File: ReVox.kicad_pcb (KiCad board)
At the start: 2 copper layers, 60.8 x 86.2 mm, 42 parts, among them CN1 EXPANSION_PORT, CN2 RAW_OUT, CN3 AMP_OUT, CN4 CN_RAW_DAC, U1 GAL20V8, U2 74LS273, U3 TLC272

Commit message: RV1 -> 500k
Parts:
- RV1: value 470k -> 500k

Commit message: C8 -> 1uF
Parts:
- C8: value 10u -> 1u

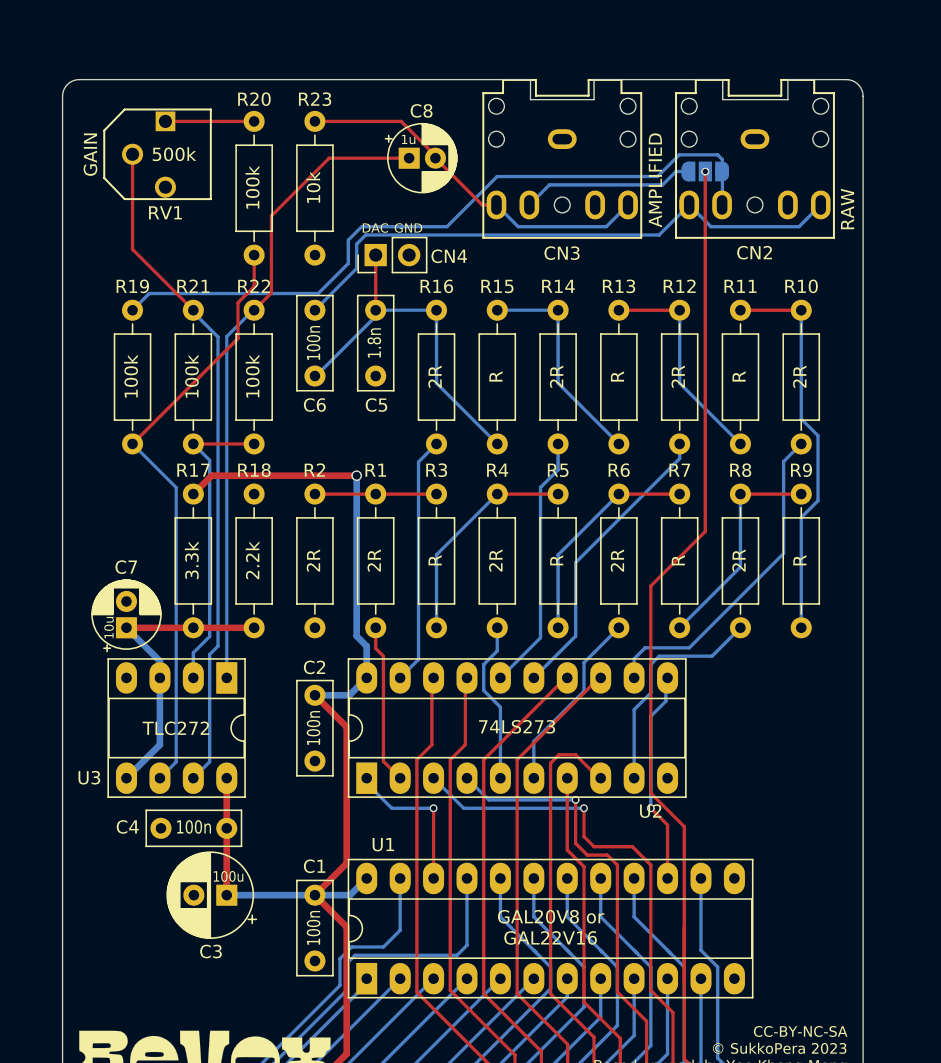
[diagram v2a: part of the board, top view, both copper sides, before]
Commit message: Remove amplified output jack This makes the opamp oscillate and is totally unnecessary
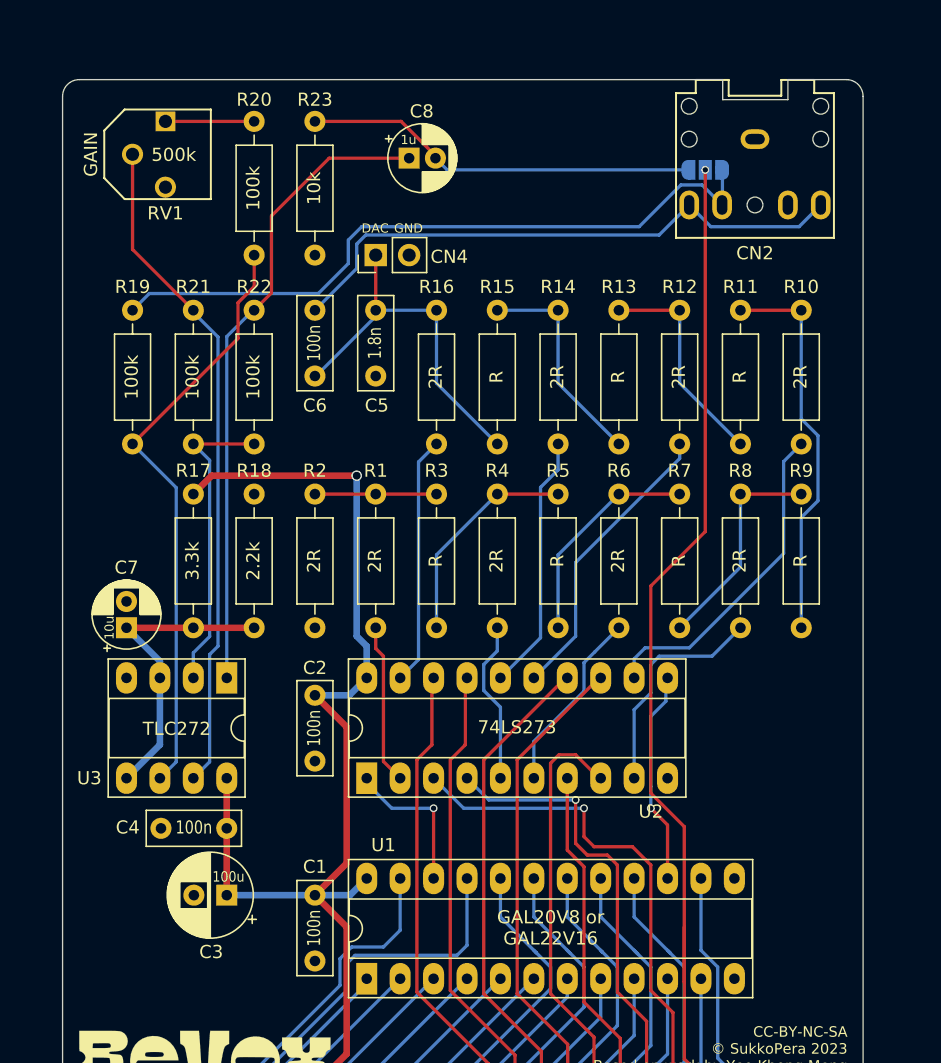
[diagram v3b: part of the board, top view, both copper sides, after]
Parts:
- removed CN3: AMP_OUT, ReVox:AudioJack_SJ1-3525N
- moved JP1 0.13 mm to (170.6, 68.7)
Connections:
- JP1 pad 1: Net-(CN3-PadTN) -> /amplified_audio
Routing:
- net Net-(CN3-PadTN): track 13.1 -> 0.00 mm
- net /amplified_audio: track 27.9 -> 30.1 mm
- net /amplifier_in: track 54.4 -> 53.0 mm
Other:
- outline, holes or cut-outs redrawn
- board text removed: "AMPLIFIED"

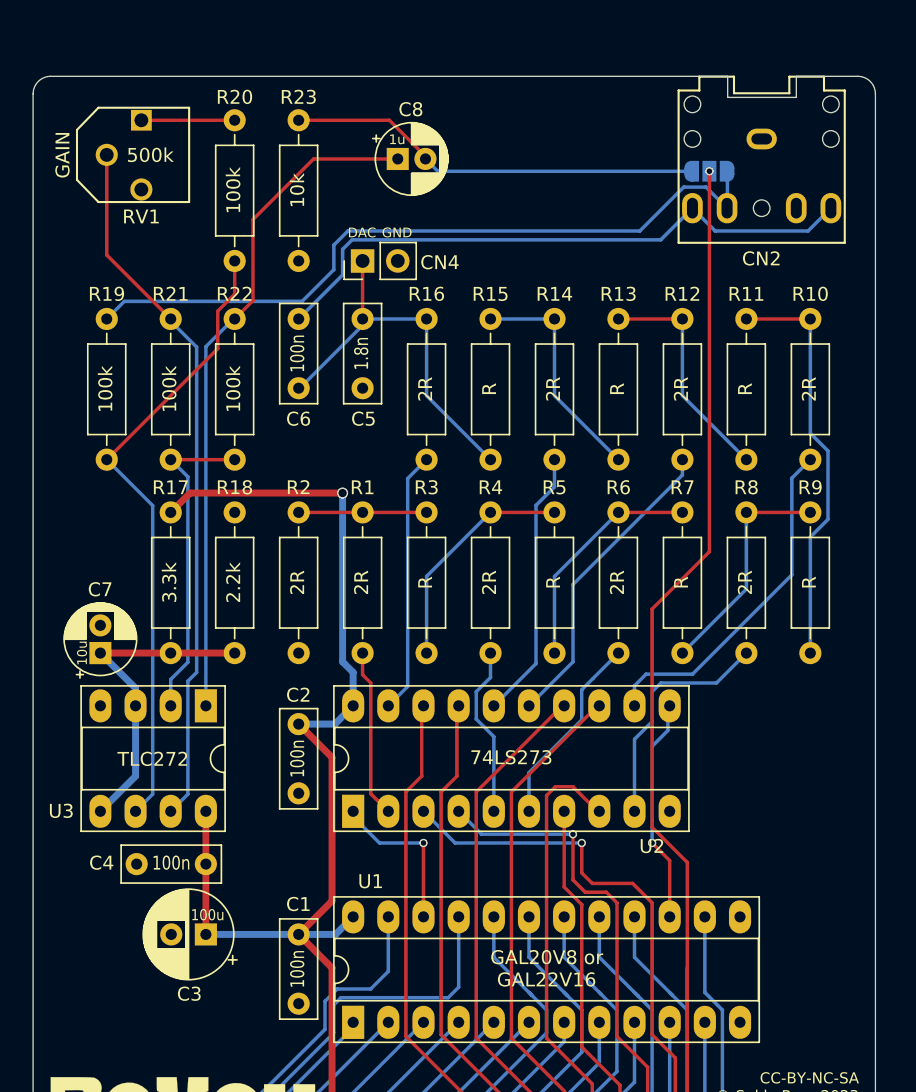
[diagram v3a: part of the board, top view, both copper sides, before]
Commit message: Some rerouting
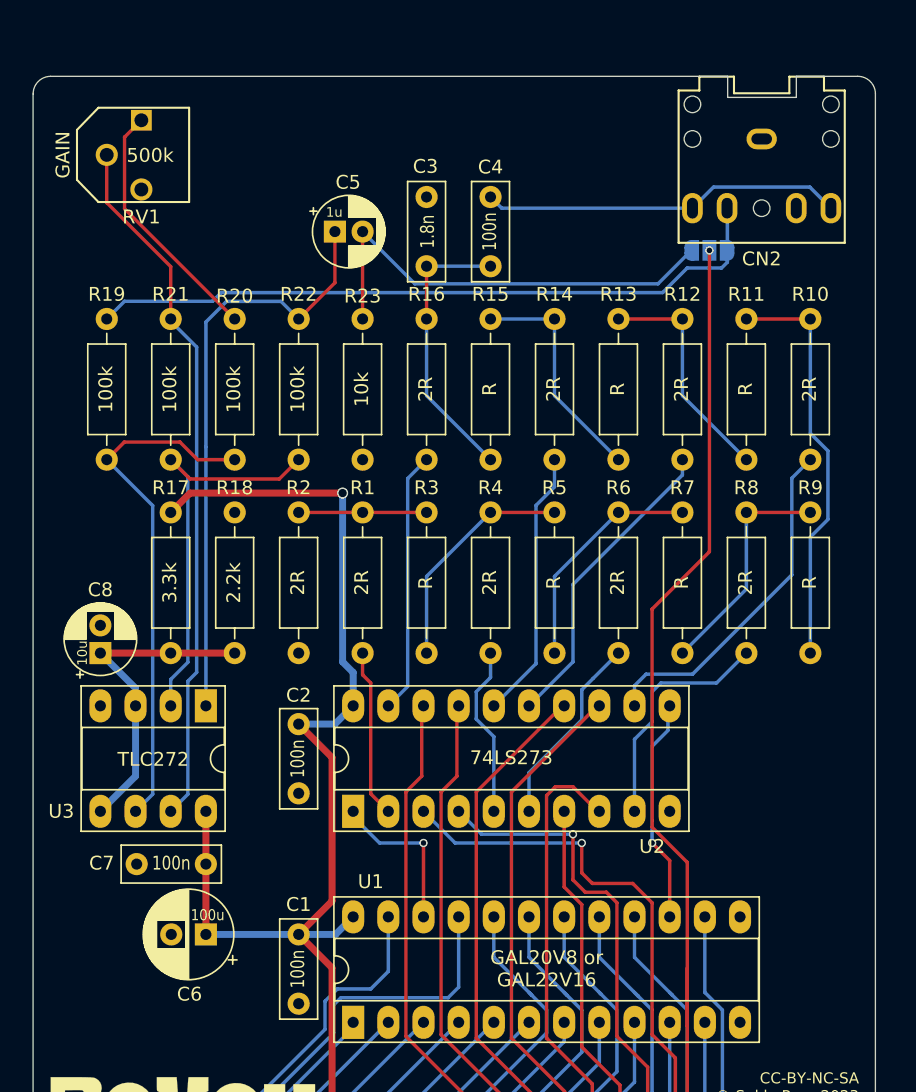
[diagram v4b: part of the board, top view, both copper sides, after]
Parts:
- removed CN4: CN_RAW_DAC, Connector_PinHeader_2.54mm:PinHeader_1x02_P2.54mm_Vertical
- moved C4 16.4 mm to (154.8, 70.6)
- moved R23 15.1 mm to (145.6, 79.4)
- moved C3 14.6 mm to (150.2, 70.6), turned to 270 degrees
- moved R20 14.4 mm to (136.4, 79.4)
- moved C5 6.94 mm to (143.6, 73.1)
- moved JP1 5.72 mm to (170.6, 74.4)
- moved R22 4.62 mm to (141.0, 79.4)
- renumbered C5 to C3, C6 to C4, C8 to C5, C3 to C6, C4 to C7, C7 to C8
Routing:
- net /analog_audio: track 44.2 -> 26.2 mm
- net Net-(R20-Pad1): track 6.74 -> 18.2 mm
- net Net-(R19-Pad1): track 45.5 -> 37.6 mm
- net Net-(C3-Pad2): track 27.8 -> 20.5 mm
- net Net-(R21-Pad2): track 23.4 -> 29.2 mm
- net /ext_audio: track 83.6 -> 77.9 mm
- net Net-(C5-Pad1): track 48.3 -> 43.0 mm
- net /amplified_audio: track 30.1 -> 32.6 mm
- net /amplifier_in: track 53.0 -> 50.4 mm
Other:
- board text removed: "DAC"
- board text removed: "GND"

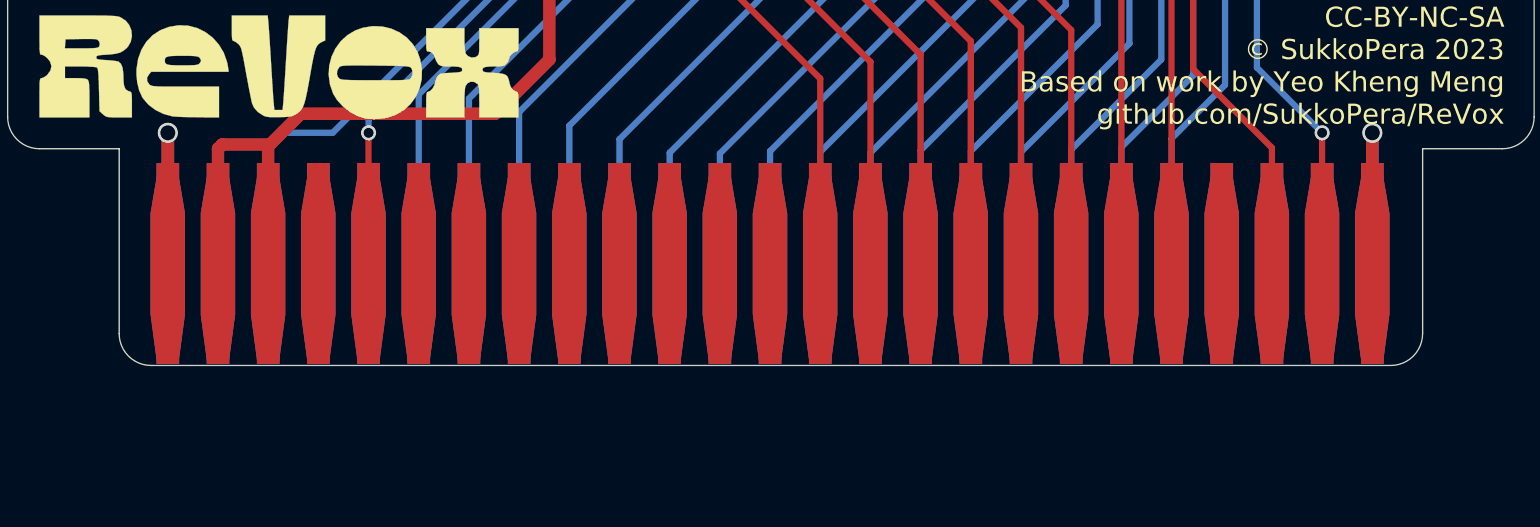
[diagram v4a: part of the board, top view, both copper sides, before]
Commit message: Update edge connector
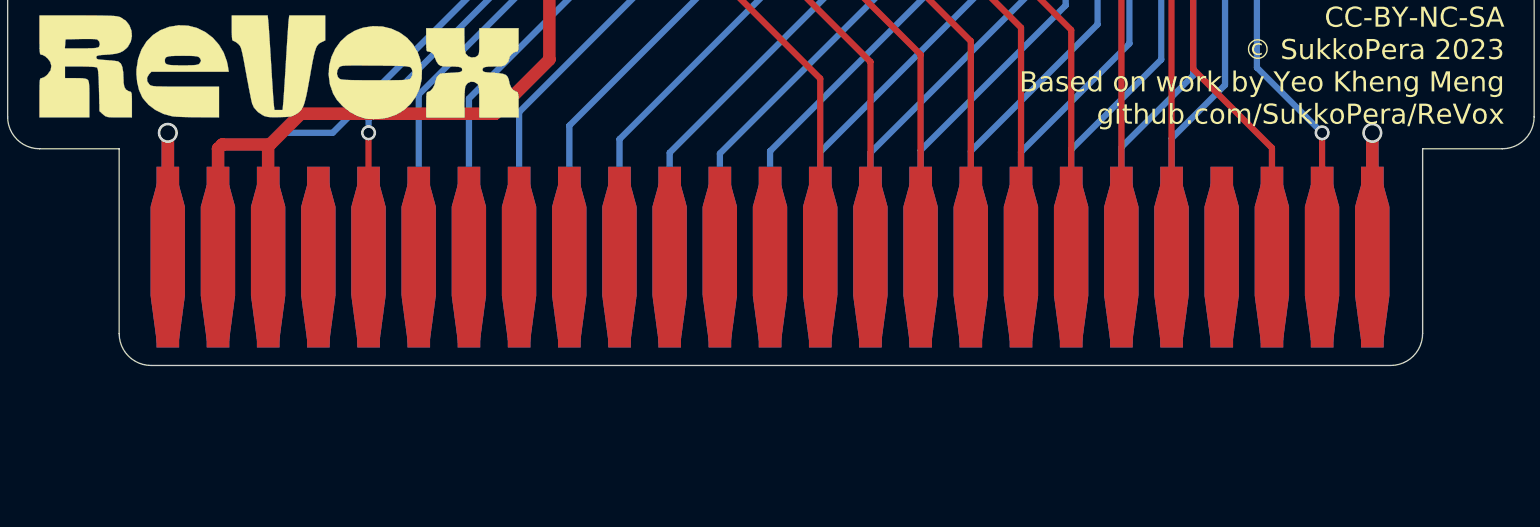
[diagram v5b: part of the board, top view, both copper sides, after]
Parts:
- moved CN1 0.25 mm to (152.2, 143.8)
